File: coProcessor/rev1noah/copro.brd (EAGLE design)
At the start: 101.6 x 101.6 mm, 0 parts

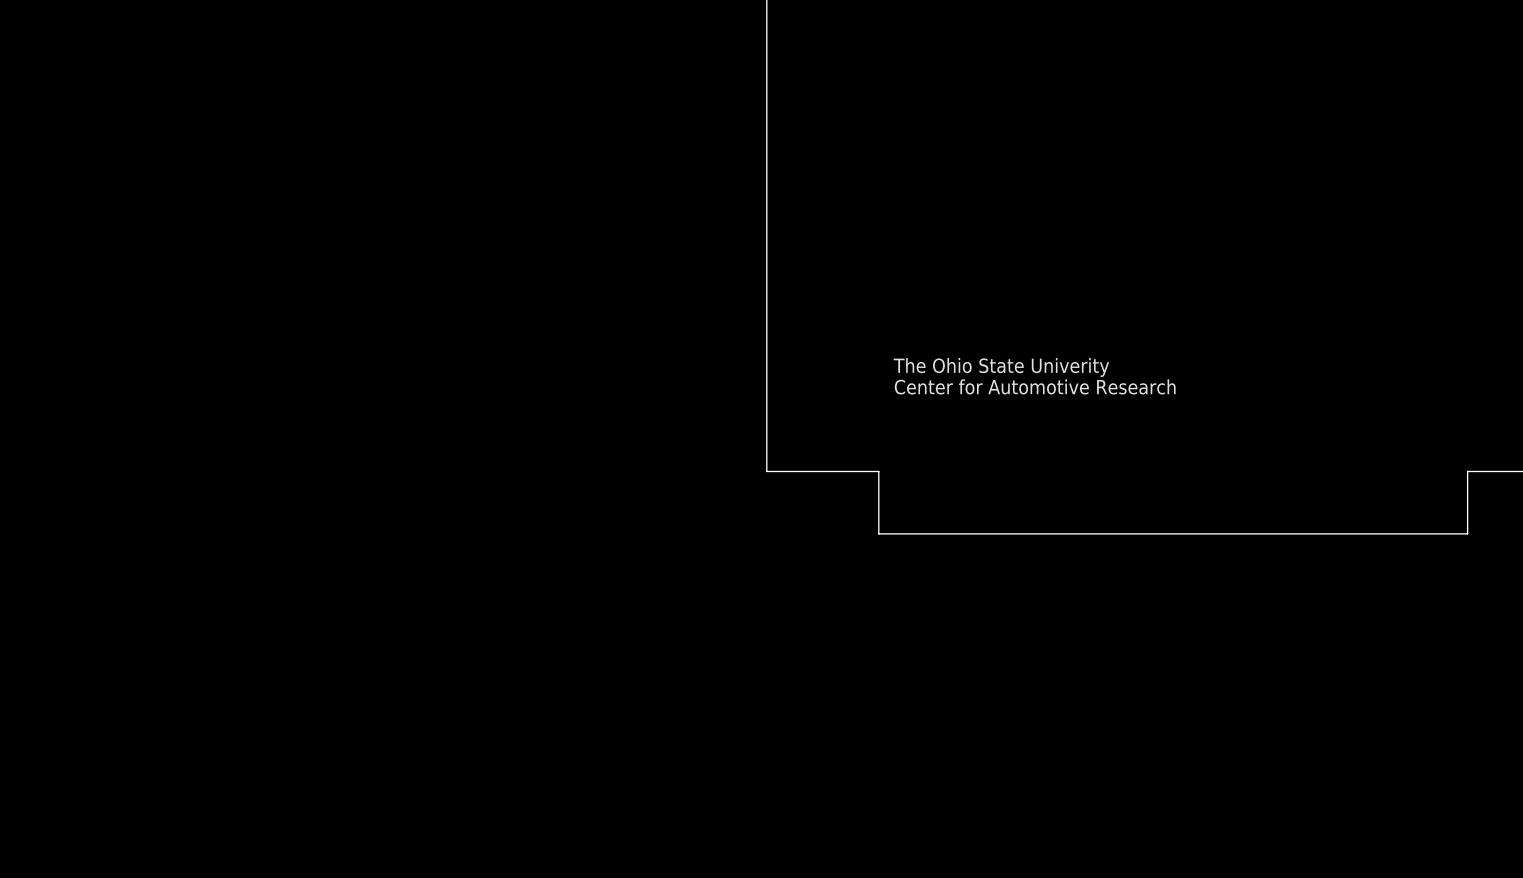
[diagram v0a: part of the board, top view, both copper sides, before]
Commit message: added several eagle libraries, all "big" parts are on the copro schematic
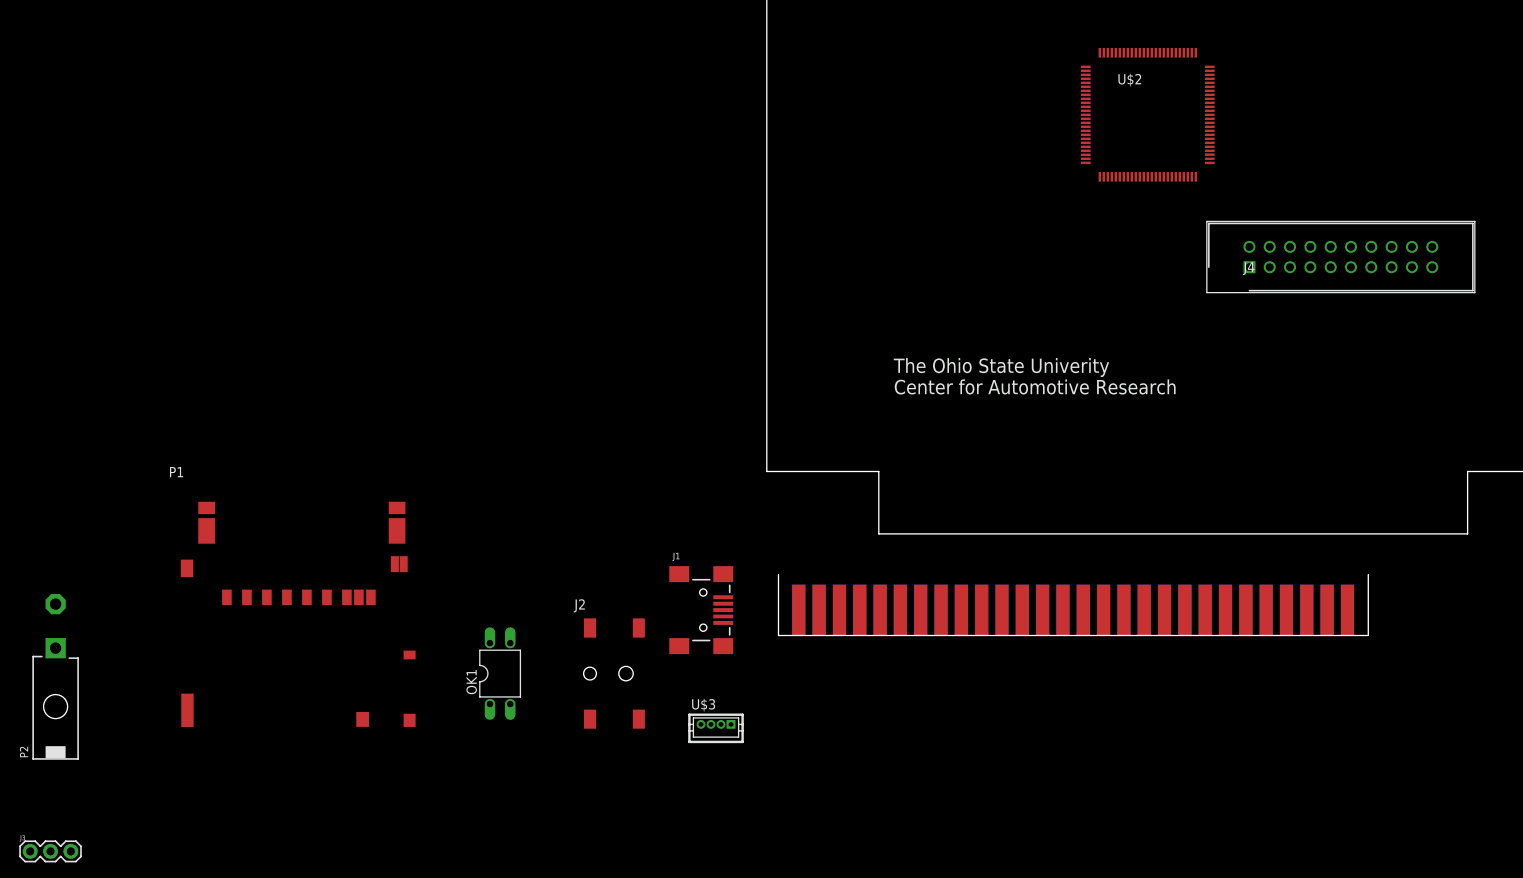
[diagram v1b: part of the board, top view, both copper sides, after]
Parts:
- added J1: USB_MINI-B_SMT, SparkFun-Connectors:USB-MINIB
- added J2: PJ-002AH-SMT-TR, PJ-002AH-SMT-TR:CUI_PJ-002AH-SMT-TR
- added J3: 455-1750-1-ND, SparkFun-Connectors:1X03
- added J4: 30320-6002HB, 30320-6002HB:SHDR20W81P254_2X10_3300X840X93
- added OK1: SFH610, optocoupler:DIL04
- added P1: 503500-0991, 503500-0991:MOLEX_503500-0991
- added P2: 39-30-02?, con-molex-mini-fit:39-30-?02?
- added U$1: 5530843, 5530843-6:5530843-6-BOARDFINGERS
- added U$2: STM32F4V_100PIN_GENERIC, stm32f4:LQFP100
- added U$3: DF13-4P-1.25DSA, con-hirose-df13:DF13-4P-1.25DSA
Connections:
- new net GND: J1.GND, U$1.GND1, U$1.GND2, U$1.GND3, U$1.GND_4, U$1.GND_5, U$1.GND_6
- new net N$1: U$1.3.3VP1, U$1.3.3VP2, U$1.3.3VP3
- new net POWER: U$1.3.3V_4, U$1.3.3V_5, U$1.3.3V_6
- new net VBUS: J1.VBUS

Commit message: some progress on the copro eagle schematic, optoisolator needs fixed
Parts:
- removed U$2: STM32F4V_100PIN_GENERIC, stm32f4:LQFP100
- added C1: 4.7uF, SparkFun-Capacitors:0603
- added C12, C2, C4, C6, C9: 100nF, SparkFun-Capacitors:0603
- added C14: 1uF, SparkFun-Capacitors:0603
- added C3, C8: 2.2uF, SparkFun-Capacitors:0603
- added IC1: STM32F405RGT6, STM32F405RGT6:QFP50P1200X1200X160-64N
- added R2, R3: 10k, SparkFun-Resistors:0603
- added R4: 1k, SparkFun-Resistors:0603
- added R5: 220, SparkFun-Resistors:0603
- added T1: 2N2222, transistor:TO18
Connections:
- new net +3V3: C14.2, C6.2, IC1.1, IC1.13
- new net 3.3V: C1.1, C12.1, C2.1, C4.1, C9.1, IC1.19, IC1.32, IC1.48, IC1.64, U$1.3.3VP1, U$1.3.3VP2, U$1.3.3VP3
- new net N$2: R4.1, T1.2
- new net N$3: C3.1, C8.1, IC1.31, IC1.47
- new net N$4: OK1.1, R5.2
- new net N$5: J3.1, R3.2
- new net N$6: OK1.3, R3.1, R4.2
- new net N$7: J3.3, T1.1
- new net N$8: R2.2
- net GND: now also C1.2, C12.2, C14.1, C2.2, C3.2, C4.2, C6.1, C8.2, C9.2, IC1.12, IC1.18, IC1.63, OK1.4
- net N$1: now also J3.2, R2.1, T1.3; no longer U$1.3.3VP1, U$1.3.3VP2, U$1.3.3VP3

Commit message: Opto-isolator finished, usb port finished, jtag finished
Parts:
- added 455-1750-1-ND1, 455-1750-1-ND2, 455-1750-1-ND3, 455-1750-1-ND4, 455-1750-1-ND5, 455-1750-1-ND6, 455-1750-1-ND7, 455-1750-1-ND8, 455-1750-1-ND9: (no value), SparkFun-Connectors:1X03
- added OK10, OK2, OK3, OK4, OK5, OK6, OK7, OK8, OK9: SFH610, optocoupler:DIL04
- added R1, R12, R13, R16, R17, R20, R21, R24, R25, R28, R29, R32, R33, R36, R37, R40, R8, R9: 10k, SparkFun-Resistors:0603
- added R10, R14, R18, R22, R26, R30, R34, R38, R6: 1k, SparkFun-Resistors:0603
- added R11, R15, R19, R23, R27, R31, R35, R39, R7: 220, SparkFun-Resistors:0603
- added T10, T2, T3, T4, T5, T6, T7, T8, T9: 2N2222, transistor:TO18
- 455-1750-1-ND: value 455-1750-1-ND -> (none)
- renumbered J3 to 455-1750-1-ND
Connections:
- removed net VBUS: J1.VBUS
- new net N$10: 455-1750-1-ND1.3, OK2.4, T2.1
- new net N$11: OK2.1, R7.2
- new net N$12: 455-1750-1-ND1.1, R8.1, T2.3
- new net N$13: IC1.14, R5.1
- new net N$14: IC1.15, R7.1
- new net N$15: 455-1750-1-ND1.2, R1.2, R8.2
- new net N$16: OK3.3, R10.2, R9.1
- new net N$17: R10.1, T3.2
- new net N$18: 455-1750-1-ND2.3, OK3.4, T3.1
- new net N$19: OK3.1, R11.2
- new net N$20: 455-1750-1-ND2.1, R12.1, T3.3
- new net N$21: IC1.16, R11.1
- new net N$22: 455-1750-1-ND2.2, R12.2, R9.2
- new net N$23: OK4.3, R13.1, R14.2
- new net N$24: R14.1, T4.2
- new net N$25: 455-1750-1-ND3.3, OK4.4, T4.1
- new net N$26: OK4.1, R15.2
- new net N$27: 455-1750-1-ND3.1, R16.1, T4.3
- new net N$28: IC1.17, R15.1
- new net N$29: 455-1750-1-ND3.2, R13.2, R16.2
- new net N$30: OK5.3, R17.1, R18.2
- new net N$31: R18.1, T5.2
- new net N$32: 455-1750-1-ND4.3, OK5.4, T5.1
- new net N$33: OK5.1, R19.2
- new net N$34: 455-1750-1-ND4.1, R20.1, T5.3
- new net N$35: IC1.22, R19.1
- new net N$36: 455-1750-1-ND4.2, R17.2, R20.2
- new net N$37: OK6.3, R21.1, R22.2
- new net N$38: R22.1, T6.2
- new net N$39: 455-1750-1-ND5.3, OK6.4, T6.1
- new net N$40: OK6.1, R23.2
- new net N$41: 455-1750-1-ND5.1, R24.1, T6.3
- new net N$42: IC1.23, R23.1
- new net N$43: 455-1750-1-ND5.2, R21.2, R24.2
- new net N$44: OK7.3, R25.1, R26.2
- new net N$45: R26.1, T7.2
- new net N$46: 455-1750-1-ND6.3, OK7.4, T7.1
- new net N$47: OK7.1, R27.2
- new net N$48: 455-1750-1-ND6.1, R28.1, T7.3
- new net N$49: IC1.26, R27.1
- new net N$50: 455-1750-1-ND6.2, R25.2, R28.2
- new net N$51: OK8.3, R29.1, R30.2
- new net N$52: R30.1, T8.2
- new net N$53: 455-1750-1-ND7.3, OK8.4, T8.1
- new net N$54: OK8.1, R31.2
- new net N$55: 455-1750-1-ND7.1, R32.1, T8.3
- new net N$56: IC1.27, R31.1
- new net N$57: 455-1750-1-ND7.2, R29.2, R32.2
- new net N$58: OK9.3, R33.1, R34.2
- new net N$59: R34.1, T9.2
- new net N$60: 455-1750-1-ND8.3, OK9.4, T9.1
- new net N$61: OK9.1, R35.2
- new net N$62: 455-1750-1-ND8.1, R36.1, T9.3
- new net N$63: IC1.29, R35.1
- new net N$64: 455-1750-1-ND8.2, R33.2, R36.2
- new net N$65: OK10.3, R37.1, R38.2
- new net N$66: R38.1, T10.2
- new net N$67: 455-1750-1-ND9.3, OK10.4, T10.1
- new net N$68: OK10.1, R39.2
- new net N$69: 455-1750-1-ND9.1, R40.1, T10.3
- new net N$70: IC1.30, R39.1
- new net N$71: 455-1750-1-ND9.2, R37.2, R40.2
- new net N$72: IC1.35, J1.D-
- new net N$73: IC1.36, J1.D+
- new net N$74: IC1.7, J4.15
- new net N$75: IC1.55, J4.13
- new net N$76: IC1.49, J4.9
- new net N$77: IC1.50, J4.7
- new net N$78: IC1.46, J4.5
- new net N$79: IC1.56, J4.3
- new net N$9: R6.1, T2.2
- net +3V3: now also J1.VBUS, J4.1, J4.2
- net GND: now also J1.S1, J1.S2, J1.S3, J1.S4, J4.10, J4.12, J4.14, J4.16, J4.18, J4.20, J4.4, J4.6, J4.8, OK1.2, OK10.2, OK2.2, OK3.2, OK4.2, OK5.2, OK6.2, OK7.2, OK8.2, OK9.2; no longer OK1.4
- net N$1: now also OK2.3, R1.1, R6.2; no longer 455-1750-1-ND.2, R2.1, T1.3
- net N$5: now also R2.1, T1.3; no longer R3.2
- net N$7: now also OK1.4
- net N$8: now also 455-1750-1-ND.2, R3.2

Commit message: copro board schematic nearly finished. Still need to work out transceiver
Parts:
- removed OK1, OK10, OK2, OK3, OK4, OK5, OK6, OK7, OK8, OK9: SFH610, optocoupler:DIL04
- removed P1: 503500-0991, 503500-0991:MOLEX_503500-0991
- removed P2: 39-30-02?, con-molex-mini-fit:39-30-?02?
- removed U$3: DF13-4P-1.25DSA, con-hirose-df13:DF13-4P-1.25DSA
- added DEPTH_SENSOR: DF13-4P-1.25DSA, con-hirose-df13:DF13-4P-1.25DSA
- added HEARTBEAT1, HEARTBEAT2: LTST-S270GKT, LTST-S270GKT:0603
- added J3: 693061010911, 693061010911:693061010911
- added OI1, OI10, OI2, OI3, OI4, OI5, OI6, OI7, OI8, OI9: SFH610, optocoupler:DIL04
- added POWERJACK: PJ-002AH-SMT-TR, PJ-002AH-SMT-TR:CUI_PJ-002AH-SMT-TR
- added R41, R42: 2.2k, SparkFun-Resistors:0603
- added R43, R44: 330, SparkFun-Resistors:0603
- added RESET_SWITCH: (no value), switch:REKN
- added SWITCH1: 39-30-02?, con-molex-mini-fit:39-30-?02?
- added U1: LM2597N-5.0, LM2597N-5.0:DIP254P762X508-8
- added U2: SN65HVD232QD, SN65HVD232QD:SOIC127P600X175-8N
- J2: value PJ-002AH-SMT-TR -> 79107-08; device PJ-002AH-SMT-TR:CUI_PJ-002AH-SMT-TR -> con-molex-milli-grid:79107-08
- moved R26 967.4 mm to (331.8, 266.7)
- moved R27 967.4 mm to (308.0, 249.2)
- moved R30 967.4 mm to (331.8, 204.8)
- moved R31 967.4 mm to (308.0, 187.3)
- moved R34 967.4 mm to (331.8, 142.9)
- moved R35 967.4 mm to (308.0, 125.4)
- moved R39 967.4 mm to (308.0, 63.5)
- moved 455-1750-1-ND6 967.4 mm to (314.3, 277.8)
- moved 455-1750-1-ND7 967.4 mm to (314.3, 215.9)
- moved 455-1750-1-ND8 967.4 mm to (314.3, 154.0)
- moved 455-1750-1-ND9 967.4 mm to (314.3, 92.1)
- moved R25 967.4 mm to (325.4, 266.7)
- moved R28 967.4 mm to (314.3, 249.2)
- moved R29 967.4 mm to (325.4, 204.8)
- moved R32 967.4 mm to (314.3, 187.3)
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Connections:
- net N$14 renamed OI2
- net N$21 renamed OI3
- net N$28 renamed OI4
- net N$35 renamed OI5
- net N$42 renamed OI6
- net N$49 renamed OI7
- net N$56 renamed OI8
- net N$63 renamed OIO9
- net N$70 renamed OI10
- net N$72 renamed D-
- net N$73 renamed D+
- net N$75 renamed JTAG13
- net N$76 renamed JTAG9
- net N$77 renamed PA15
- net N$78 renamed JTAG5
- net N$79 renamed JTAG3
- removed net N$34: 455-1750-1-ND4.1, R20.1, T5.3
- removed net N$39: 455-1750-1-ND5.3, OK6.4, T6.1
- removed net N$41: 455-1750-1-ND5.1, R24.1, T6.3
- removed net N$46: 455-1750-1-ND6.3, OK7.4, T7.1
- removed net N$48: 455-1750-1-ND6.1, R28.1, T7.3
- removed net N$53: 455-1750-1-ND7.3, OK8.4, T8.1
- removed net N$55: 455-1750-1-ND7.1, R32.1, T8.3
- removed net N$60: 455-1750-1-ND8.3, OK9.4, T9.1
- removed net N$62: 455-1750-1-ND8.1, R36.1, T9.3
- removed net N$67: 455-1750-1-ND9.3, OK10.4, T10.1
- removed net N$69: 455-1750-1-ND9.1, R40.1, T10.3
- removed net N$74: IC1.7, J4.15
- new net CLK: IC1.53, J3.5
- new net CMD: IC1.54, J3.2
- new net DATO: IC1.39, J3.7
- new net GNDA: 455-1750-1-ND1.3, 455-1750-1-ND2.3, 455-1750-1-ND3.3, 455-1750-1-ND4.3, 455-1750-1-ND5.3, 455-1750-1-ND6.3, 455-1750-1-ND7.3, 455-1750-1-ND8.3, 455-1750-1-ND9.3, OI10.4, OI2.4, OI3.4, OI4.4, OI5.4, OI6.4, OI7.4, OI8.4, OI9.4, SWITCH1.1, T10.1, T2.1, T3.1, T4.1, T5.1, T6.1, T7.1, T8.1, T9.1
- new net GNDBAT: 455-1750-1-ND.3, OI1.4, T1.1
- new net HEARTBEAT1: IC1.37, R44.1
- new net HEARTBEAT2: IC1.38, R43.1
- new net JTAG15: IC1.7, J4.15, RESET_SWITCH.1A, RESET_SWITCH.1B
- new net N$14: HEARTBEAT2.2, R43.2
- new net N$21: J3.3, J3.6, J3.Z1, J3.Z2
- new net N$28: HEARTBEAT1.2, R44.2
- new net PB8: DEPTH_SENSOR.P$2, IC1.61, R41.1
- new net PS$3: DEPTH_SENSOR.P$3, IC1.62, R42.1
- new net TXD: IC1.45, U2.1
- net +3V3: now also C1.1, C12.1, C2.1, C4.1, C9.1, DEPTH_SENSOR.P$1, IC1.19, IC1.32, IC1.48, IC1.64, J2.1, J2.3, J2.5, J2.7, J3.4, POWERJACK.1.1, POWERJACK.1.2, R41.2, R42.2, U2.3; no longer IC1.1
- net 3.3V: no longer C1.1, C12.1, C2.1, C4.1, C9.1, IC1.19, IC1.32, IC1.48, IC1.64
- net GND: now also DEPTH_SENSOR.P$4, HEARTBEAT1.1, HEARTBEAT2.1, OI1.2, OI10.2, OI2.2, OI3.2, OI4.2, OI5.2, OI6.2, OI7.2, OI8.2, OI9.2, POWERJACK.2, POWERJACK.3, RESET_SWITCH.0B, U1.6, U2.2; no longer OK1.2, OK10.2, OK2.2, OK3.2, OK4.2, OK5.2, OK6.2, OK7.2, OK8.2, OK9.2
- net N$1: now also OI2.3; no longer OK2.3
- net N$10: now also R2.2, R3.2; no longer 455-1750-1-ND1.3, OK2.4, T2.1
- net N$11: now also OI2.1; no longer OK2.1
- net N$12: now also U$1.CAN_L, U2.6; no longer 455-1750-1-ND1.1, R8.1, T2.3
- net N$15: no longer 455-1750-1-ND1.2
- net N$16: now also OI3.3; no longer OK3.3
- net N$18: now also 455-1750-1-ND.1, 455-1750-1-ND1.1, 455-1750-1-ND2.1, 455-1750-1-ND3.1, 455-1750-1-ND4.1, 455-1750-1-ND5.1, 455-1750-1-ND6.1, 455-1750-1-ND7.1, 455-1750-1-ND8.1, 455-1750-1-ND9.1, R12.1, R16.1, R2.1, R20.1, R24.1, R28.1, R32.1, R36.1, R40.1, R8.1, T1.3, T10.3, T2.3, T3.3, T4.3, T5.3, T6.3, T7.3, T8.3, T9.3, U1.8; no longer 455-1750-1-ND2.3, OK3.4, T3.1
- net N$19: now also OI3.1; no longer OK3.1
- net N$20: now also IC1.8, J2.2; no longer 455-1750-1-ND2.1, R12.1, T3.3
- net N$22: no longer 455-1750-1-ND2.2
- net N$23: now also OI4.3; no longer OK4.3
- net N$25: now also IC1.9, J2.4; no longer 455-1750-1-ND3.3, OK4.4, T4.1
- net N$26: now also OI4.1; no longer OK4.1
- net N$27: now also IC1.10, J2.6; no longer 455-1750-1-ND3.1, R16.1, T4.3
- net N$29: no longer 455-1750-1-ND3.2
- net N$30: now also OI5.3; no longer OK5.3
- net N$32: now also IC1.11, J2.8; no longer 455-1750-1-ND4.3, OK5.4, T5.1
- net N$33: now also OI5.1; no longer OK5.1
- net N$36: no longer 455-1750-1-ND4.2
- net N$37: now also OI6.3; no longer OK6.3
- net N$4: now also OI1.1; no longer OK1.1
- net N$40: now also OI6.1; no longer OK6.1
- net N$43: no longer 455-1750-1-ND5.2
- net N$44: now also OI7.3; no longer OK7.3
- net N$47: now also OI7.1; no longer OK7.1
- net N$5: now also IC1.44, U2.4; no longer 455-1750-1-ND.1, R2.1, T1.3
- net N$50: no longer 455-1750-1-ND6.2
- net N$51: now also OI8.3; no longer OK8.3
- net N$54: now also OI8.1; no longer OK8.1
- net N$57: no longer 455-1750-1-ND7.2
- net N$58: now also OI9.3; no longer OK9.3
- net N$6: now also OI1.3; no longer OK1.3
- net N$61: now also OI9.1; no longer OK9.1
- net N$64: no longer 455-1750-1-ND8.2
- net N$65: now also OI10.3; no longer OK10.3
- net N$68: now also OI10.1; no longer OK10.1
- net N$7: now also SWITCH1.2, U1.7; no longer 455-1750-1-ND.3, OK1.4, T1.1
- net N$71: no longer 455-1750-1-ND9.2
- net N$8: now also U$1.CAN_H, U2.7; no longer 455-1750-1-ND.2, R2.2, R3.2
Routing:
- net 3.3V: track 0.00 -> 5.08 mm
